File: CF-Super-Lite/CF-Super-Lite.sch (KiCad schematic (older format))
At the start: 2 parts, among them J1 Bus_ISA_8bit, J2 IDE_CONNECTOR

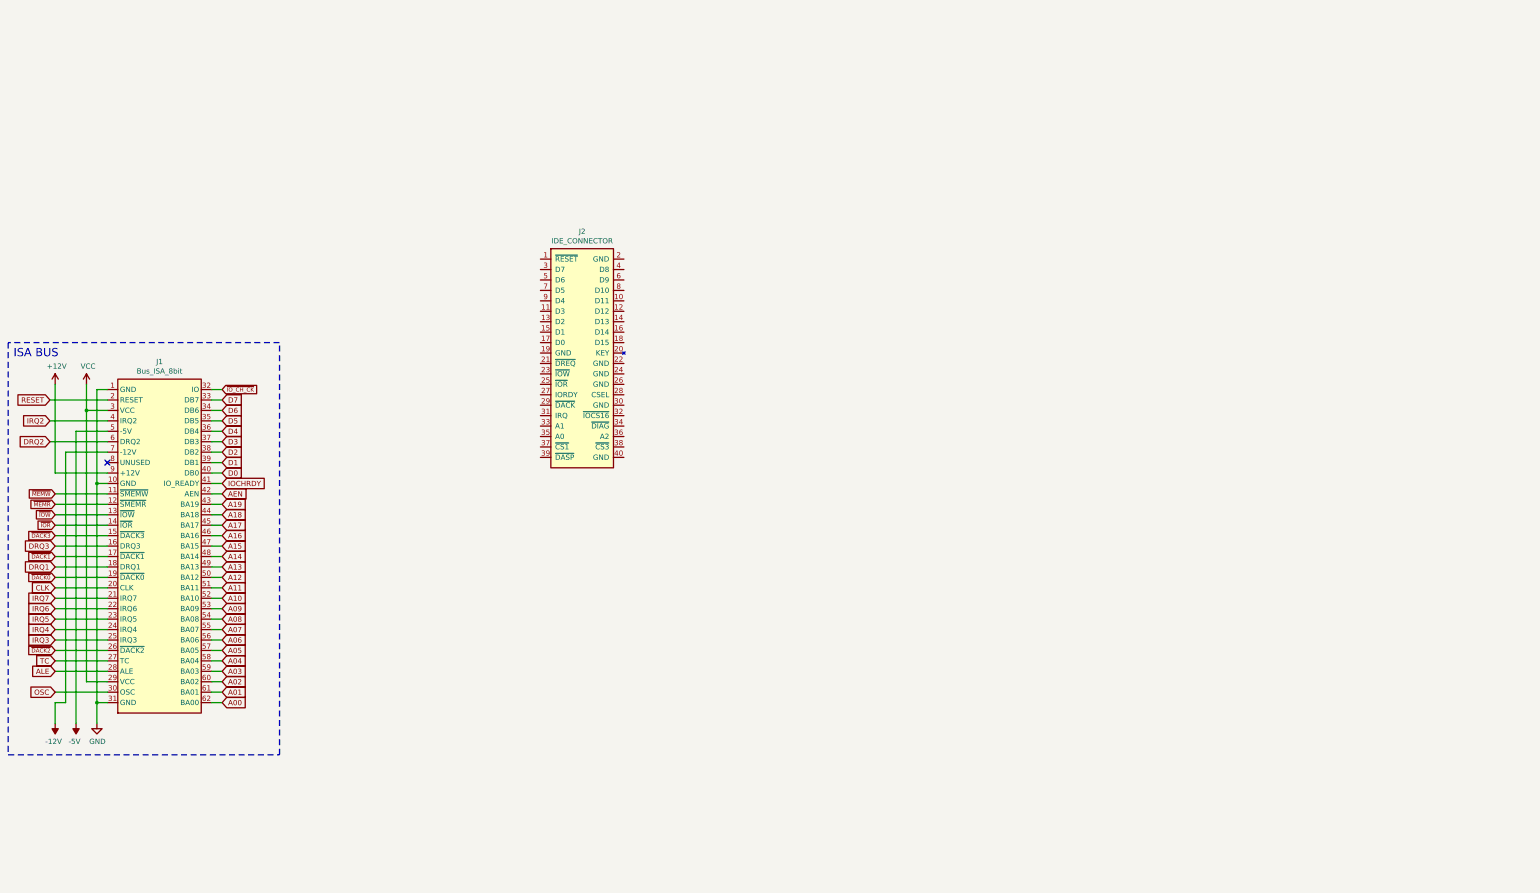
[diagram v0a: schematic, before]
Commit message: Add IC's to schematic and PCB.
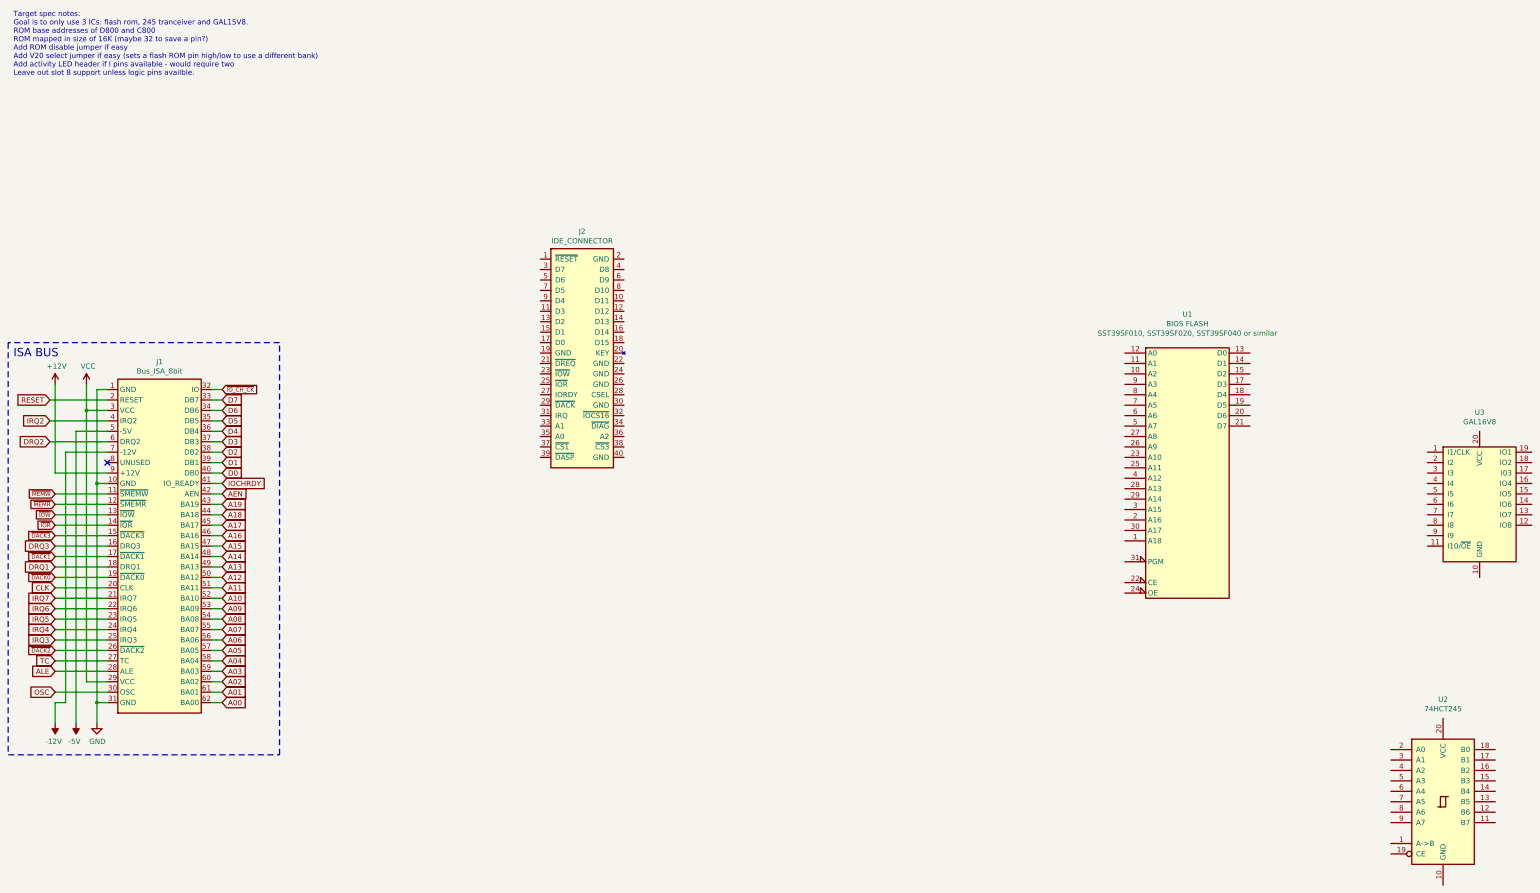
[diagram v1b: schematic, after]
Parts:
- added U1: BIOS FLASH, Package_DIP:DIP-32_W15.24mm_Socket, symbol Memory_Flash:SST39SF040
- added U2: 74HCT245, Package_DIP:DIP-20_W7.62mm_Socket, symbol 74xx:74LS245
- added U3: GAL16V8, Package_DIP:DIP-20_W7.62mm_Socket, symbol Logic_Programmable:GAL16V8
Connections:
- net GND: now also U1.16 (GND)
- net VCC: now also U1.32 (VCC)
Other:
- note added: "Target spec notes:\nGoal is to only use 3 ICs: flash rom, 245 tranceiver and GAL15V8.\nROM base addresses of D800 and C800\nROM mapped in size of 16K (maybe 32 to save a pin?)\nAdd ROM disable jumper if easy\nAdd V20 select jumper if easy (sets a flash ROM pin high/low to use a different bank)\nAdd activity LED header if l pins available - would require two\nLeave out slot 8 support unless logic 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"
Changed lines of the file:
@@
 EELAYER 30 0
 EELAYER END
-$Descr A4 11693 8268
+$Descr A2 23386 16535
 encoding utf-8
 Sheet 1 1
@@
 	1    0    0    -1
 $EndComp
+Text Notes 600  1200 0    50   ~ 0
+Target spec notes:\nGoal is to only use 3 ICs: flash rom, 245 tranceiver and GAL15V8.\nROM base addresses of D800 and C800\nROM mapped in size of 16K (maybe 32 to save a pin?)\nAdd ROM disable jumper if easy\nAdd V20 select jumper if easy (sets a flash ROM pin high/low to use a different bank)\nAdd activity LED header if l pins available - would require two\nLeave out slot 8 support unless logic pins availble.
+$Comp
+L Memory_Flash:SST39SF040 U1
+U 1 1 603B5177
+P 11850 5050
+F 0 "U1" H 11850 6621 50  0000 C CNN
+F 1 "BIOS FLASH" H 11850 6530 50  0000 C CNN
+F 2 "Package_DIP:DIP-32_W15.24mm_Socket" H 11850 5350 50  0001 C CNN
+F 3 "http://ww1.microchip.com/downloads/en/DeviceDoc/25022B.pdf" H 11850 5350 50  0001 C CNN
+F 4 "SST39SF010, SST39SF020, SST39SF040 or similar" H 11850 6439 50  0000 C CNN "Note"
+	1    11850 5050
+	1    0    0    -1
+$EndComp
+$Comp
+L 74xx:74LS245 U2
+U 1 1 603B775F
+P 14300 8150
+F 0 "U2" H 14300 9131 50  0000 C CNN
+F 1 "74HCT245" H 14300 9040 50  0000 C CNN
+F 2 "Package_DIP:DIP-20_W7.62mm_Socket" H 14300 8150 50  0001 C CNN
+F 3 "http://www.ti.com/lit/gpn/sn74LS245" H 14300 8150 50  0001 C CNN
+	1    14300 8150
+	1    0    0    -1
+$EndComp
+$Comp
+L Logic_Programmable:GAL16V8 U3
+U 1 1 603B89A9
+P 14650 5300
+F 0 "U3" H 14650 6181 50  0000 C CNN
+F 1 "GAL16V8" H 14650 6090 50  0000 C CNN
+F 2 "Package_DIP:DIP-20_W7.62mm_Socket" H 14650 5300 50  0001 C CNN
+F 3 "" H 14650 5300 50  0001 C CNN
+	1    14650 5300
+	1    0    0    -1
+$EndComp

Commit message: CF-Super-Lite: Label most IC pins and IDE connector.
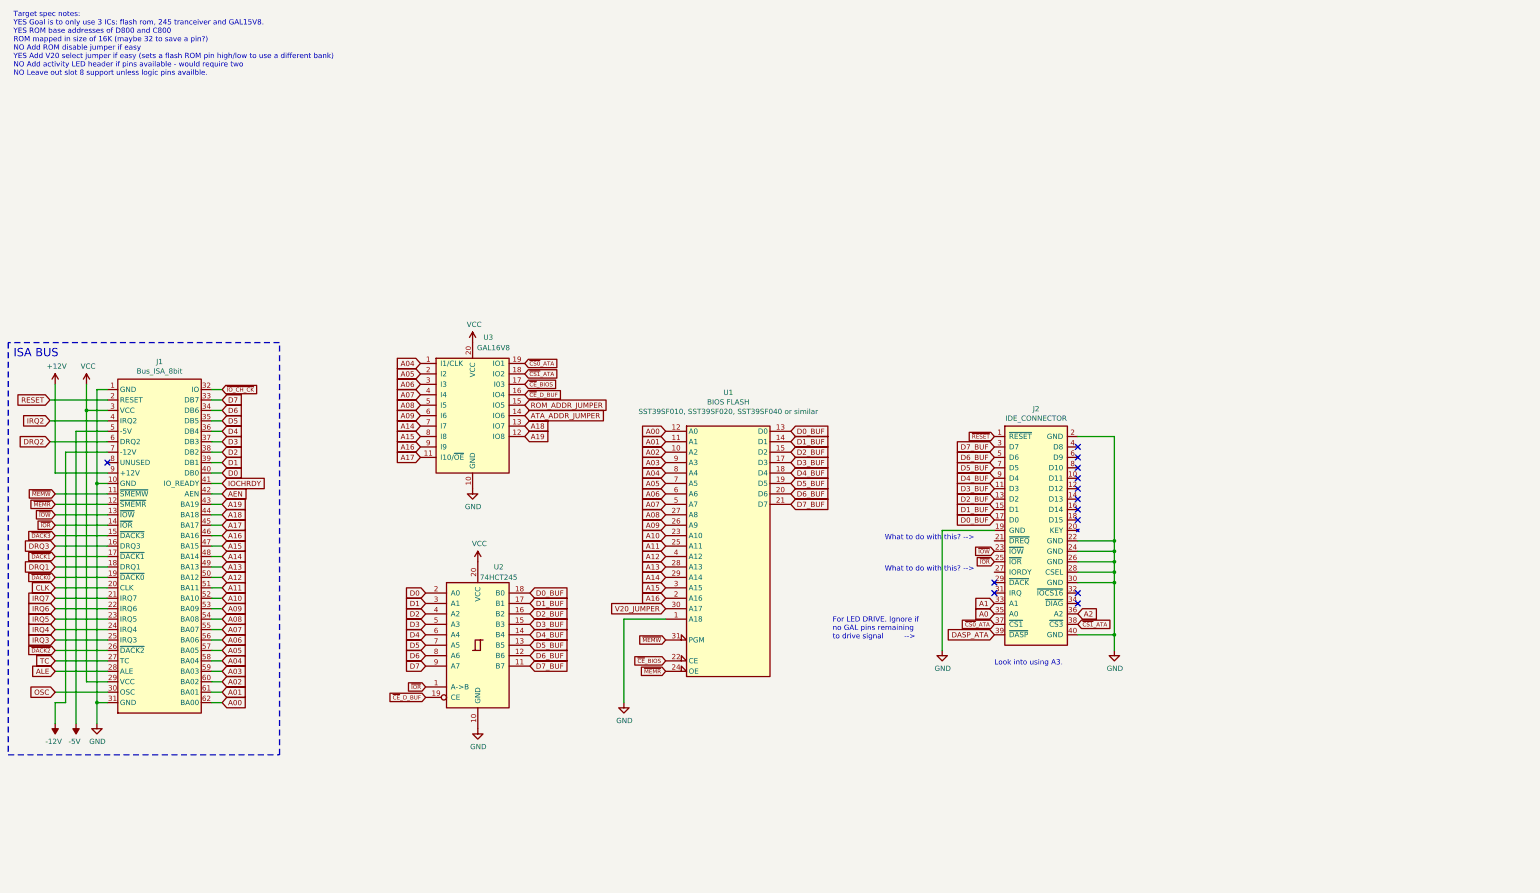
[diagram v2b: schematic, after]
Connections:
- net A00: now also U1.12 (A0)
- net A01: now also U1.11 (A1)
- net A02: now also U1.10 (A2)
- net A03: now also U1.9 (A3)
- net A04: now also U1.8 (A4), U3.1 (I1/CLK)
- net A05: now also U1.7 (A5), U3.2 (I2)
- net A06: now also U1.6 (A6), U3.3 (I3)
- net A07: now also U1.5 (A7), U3.4 (I4)
- net A08: now also U1.27 (A8), U3.5 (I5)
- net A09: now also U1.26 (A9), U3.6 (I6)
- net A10: now also U1.23 (A10)
- net A11: now also U1.25 (A11)
- net A12: now also U1.4 (A12)
- net A13: now also U1.28 (A13)
- net A14: now also U1.29 (A14), U3.7 (I7)
- net A15: now also U1.3 (A15), U3.8 (I8)
- net A16: now also U1.2 (A16), U3.9 (I9)
- net A17: now also U3.11 (I10/~OE~)
- net A18: now also U3.13 (IO7)
- net A19: now also U3.12 (IO8)
- net D0: now also U2.2 (A0)
- net D1: now also U2.3 (A1)
- net D2: now also U2.4 (A2)
- net D3: now also U2.5 (A3)
- net D4: now also U2.6 (A4)
- net D5: now also U2.7 (A5)
- net D6: now also U2.8 (A6)
- net D7: now also U2.9 (A7)
- net GND: now also J2.19 (GND), J2.2 (GND), J2.22 (GND), J2.24 (GND), J2.26 (GND), J2.28 (CSEL), J2.30 (GND), J2.40 (GND), U1.1 (A18), U2.10 (GND), U3.10 (GND)
- net VCC: now also U2.20 (VCC), U3.20 (VCC)
- net ~IOR: now also J2.25 (~IOR), U2.1 (A->B)
- net ~IOW: now also J2.23 (~IOW)
- net ~MEMR: now also U1.24 (OE)
- net ~MEMW: now also U1.31 (PGM)
- net D0_BUF: now reaches U1.13 (D0)
- net D0_BUF: now also J2.17 (D0), U2.18 (B0)
- net D1_BUF: now reaches U1.14 (D1)
- net D1_BUF: now also J2.15 (D1), U2.17 (B1)
- net D2_BUF: now reaches U1.15 (D2)
- net D2_BUF: now also J2.13 (D2), U2.16 (B2)
- net D3_BUF: now reaches U1.17 (D3)
- net D3_BUF: now also J2.11 (D3), U2.15 (B3)
- net D4_BUF: now reaches U1.18 (D4)
- net D4_BUF: now also J2.9 (D4), U2.14 (B4)
- net D5_BUF: now reaches U1.19 (D5)
- net D5_BUF: now also J2.7 (D5), U2.13 (B5)
- net D6_BUF: now reaches U1.20 (D6)
- net D6_BUF: now also J2.5 (D6), U2.12 (B6)
- net D7_BUF: now reaches U1.21 (D7)
- net D7_BUF: now also J2.3 (D7), U2.11 (B7)
- net ~CE~_BIOS: now reaches U1.22 (CE)
- net ~CE~_BIOS: now also U3.17 (I03)
- net V20_JUMPER: now reaches U1.30 (A17)
- net ~CE~_D_BUF: now reaches U2.19 (CE)
- net ~CE~_D_BUF: now also U3.16 (IO4)
- net ATA_ADDR_JUMPER: now reaches U3.14 (IO6)
- net ROM_ADDR_JUMPER: now reaches U3.15 (IO5)
- net ~CS1~_ATA: now reaches U3.18 (IO2)
- net ~CS1~_ATA: now also J2.38 (~CS3)
- net ~CS0~_ATA: now reaches U3.19 (IO1)
- net ~CS0~_ATA: now also J2.37 (~CS1)
- net ~RESET: now reaches J2.1 (~RESET)
- net A1: now reaches J2.33 (A1)
- net A0: now reaches J2.35 (A0)
- net A2: now reaches J2.36 (A2)
- net DASP_ATA: now reaches J2.39 (~DASP)
- no-connect marks 1 -> 13
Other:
- note added: "For LED DRIVE. Ignore if\nno GAL pins remaining \nto drive signal -->"
- note added: "Look into using A3."
- note added: "Target spec notes:\nYES Goal is to only use 3 ICs: flash rom, 245 tranceiver and GAL15V8.\nYES ROM base addresses of D800 and C800\nROM mapped in size of 16K (maybe 32 to save a pin?)\nNO Add ROM disable jumper if easy\nYES Add V20 select jumper if easy (sets a flash ROM pin high/low to use a different bank)\nNO Add activity LED header if pins available - would require two\nNO Leave out slot 8 su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"
- note added: "What to do with this? -->"
- note removed: "Target spec notes:\nGoal is to only use 3 ICs: flash rom, 245 tranceiver and GAL15V8.\nROM base addresses of D800 and C800\nROM mapped in size of 16K (maybe 32 to save a pin?)\nAdd ROM disable jumper if easy\nAdd V20 select jumper if easy (sets a flash ROM pin high/low to use a different bank)\nAdd activity LED header if l pins available - would require two\nLeave out slot 8 support unless logic 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"
- moved on the sheet: J2, U1, U2, U3

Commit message: Add jumper section, tidy up schematic some more.
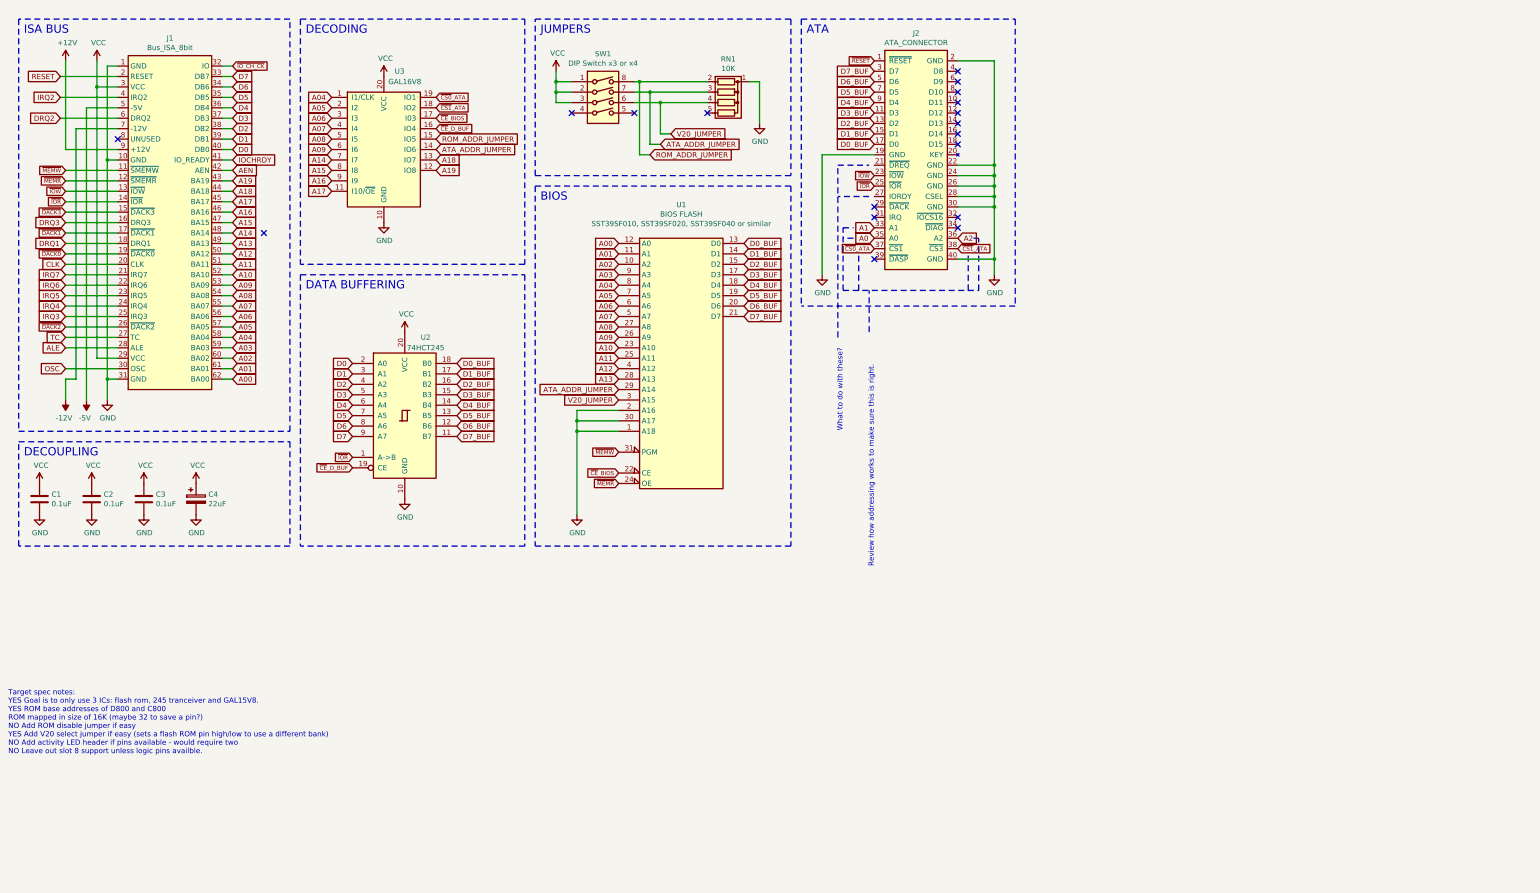
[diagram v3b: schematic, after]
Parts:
- added C1, C2, C3: 0.1uF, Capacitor_THT:C_Disc_D6.0mm_W2.5mm_P5.00mm, symbol Device:C
- added C4: 22uF, Capacitor_THT:CP_Radial_D5.0mm_P2.50mm, symbol Device:CP
- added RN1: 10K, Resistor_THT:R_Array_SIP5, symbol Device:R_Network04
- added SW1: DIP Switch x3 or x4, Button_Switch_THT:SW_DIP_SPSTx04_Slide_9.78x12.34mm_W7.62mm_P2.54mm, symbol Switch:SW_DIP_x04
- J2: value IDE_CONNECTOR -> ATA_CONNECTOR
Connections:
- net A14: no longer U1.29 (A14)
- net A15: no longer U1.3 (A15)
- net A16: no longer U1.2 (A16)
- net ATA_ADDR_JUMPER: now also U1.29 (A14), RN1.3 (R2), SW1.7
- net GND: now also U1.2 (A16), U1.30 (A17), C1.2, C2.2, C3.2, C4.2, RN1.1 (common)
- net ROM_ADDR_JUMPER: now also RN1.2 (R1), SW1.8
- net V20_JUMPER: now also U1.3 (A15), RN1.4 (R3), SW1.6; no longer U1.30 (A17)
- net VCC: now also C1.1, C2.1, C3.1, C4.1, SW1.1, SW1.2, SW1.3
- net DASP_ATA: no longer names the net of J2.39 (~DASP)
- no-connect marks 13 -> 18
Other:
- note added: "ATA"
- note added: "BIOS"
- note added: "DATA BUFFERING"
- note added: "DECODING"
- note added: "DECOUPLING"
- note added: "JUMPERS"
- note added: "Review how addressing works to make sure this is right."
- note added: "What to do with these?"
- note removed: "For LED DRIVE. Ignore if\nno GAL pins remaining \nto drive signal -->"
- note removed: "Look into using A3."
- note removed: "What to do with this? -->"
- moved on the sheet: J1, J2, U1, U2, U3

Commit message: More premature layout work.
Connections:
- net ATA_ADDR_JUMPER: now also U3.19 (IO1); no longer U3.14 (IO6)
- net ROM_ADDR_JUMPER: now also U3.18 (IO2); no longer U3.15 (IO5)
- net ~CE~_BIOS: now also U3.14 (IO6); no longer U3.17 (I03)
- net ~CE~_D_BUF: now also U3.15 (IO5); no longer U3.16 (IO4)
- net ~CS0~_ATA: now also U3.17 (I03); no longer U3.19 (IO1)
- net ~CS1~_ATA: now also U3.16 (IO4); no longer U3.18 (IO2)
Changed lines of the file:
@@
 Text GLabel 7600 3500 2    50   Input ~ 0
 D7_BUF
-Text GLabel 4650 1400 2    39   Input ~ 0
+Text GLabel 4650 1600 2    39   Input ~ 0
 ~CS0~_ATA
-Text GLabel 4650 1500 2    39   Input ~ 0
+Text GLabel 4650 1700 2    39   Input ~ 0
 ~CS1~_ATA
-Text GLabel 4650 1600 2    39   Input ~ 0
+Text GLabel 4650 1900 2    39   Input ~ 0
 ~CE~_BIOS
-Text GLabel 4650 1700 2    39   Input ~ 0
+Text GLabel 4650 1800 2    39   Input ~ 0
 ~CE~_D_BUF
 Text GLabel 2700 3500 2    50   Input ~ 0
@@
 Text GLabel 3650 2000 0    50   Input ~ 0
 A14
-Text GLabel 4650 1800 2    50   Input ~ 0
+Text GLabel 4650 1500 2    50   Input ~ 0
 ROM_ADDR_JUMPER
-Text GLabel 4650 1900 2    50   Input ~ 0
+Text GLabel 4650 1400 2    50   Input ~ 0
 ATA_ADDR_JUMPER
 Text GLabel 6400 4300 0    50   Input ~ 0
